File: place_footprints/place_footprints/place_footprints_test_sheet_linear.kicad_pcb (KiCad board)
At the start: 2 copper layers, 64 parts

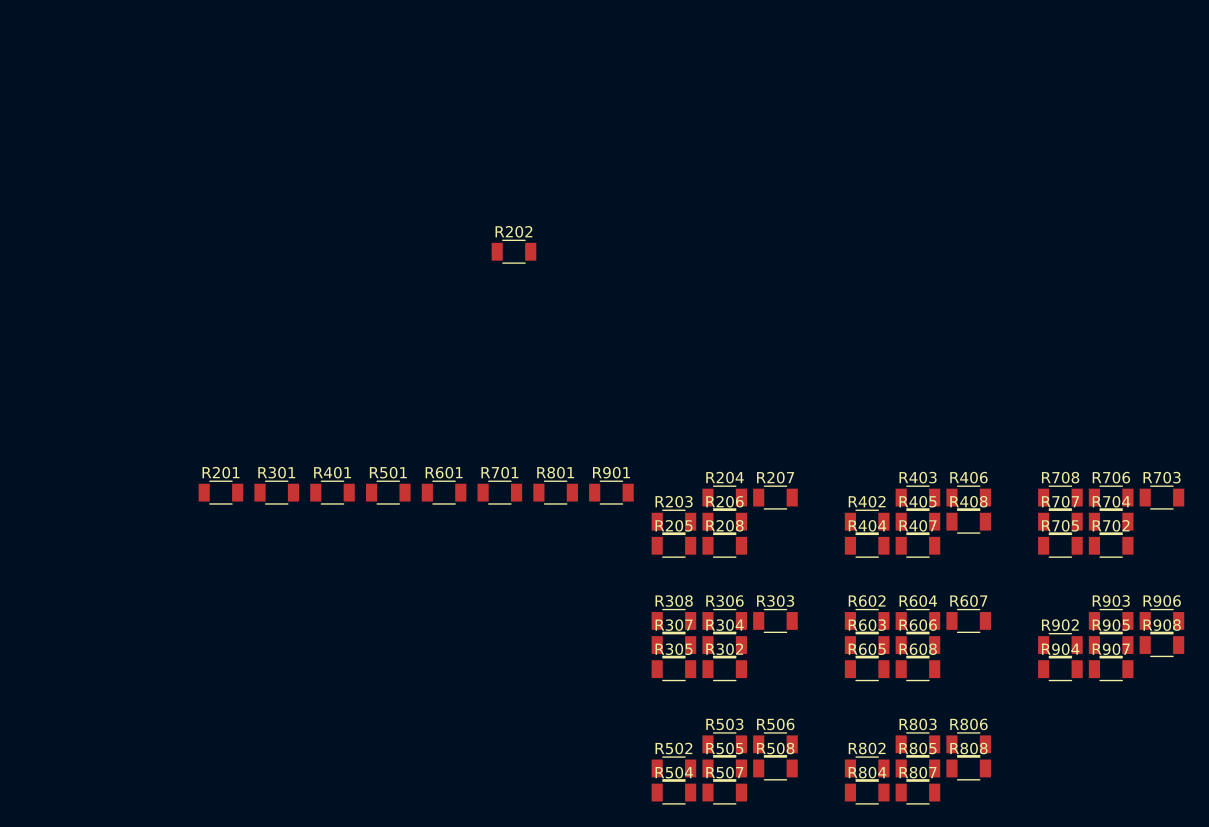
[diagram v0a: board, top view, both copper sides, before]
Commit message: Fixed circular placement
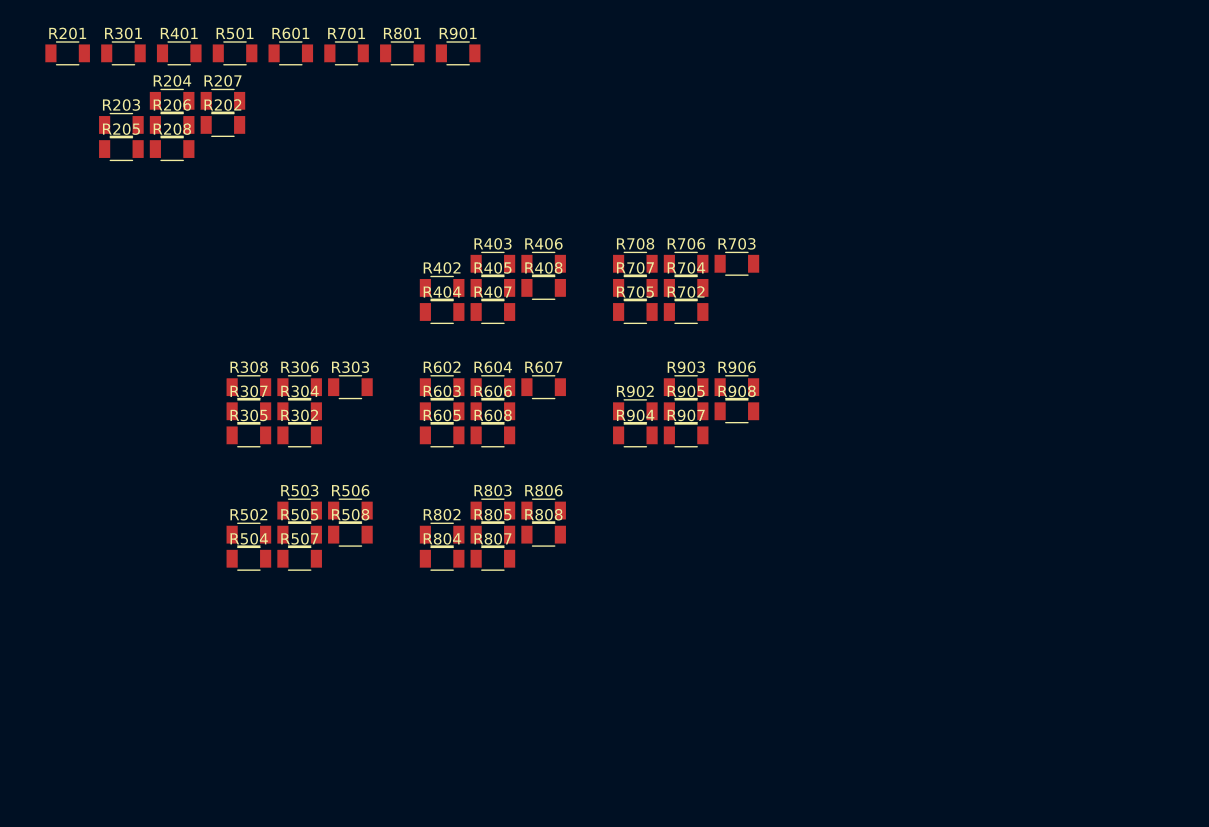
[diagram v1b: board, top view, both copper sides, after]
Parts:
- moved R204 61.0 mm to (53.2, 33.5)
- moved R206 61.0 mm to (53.2, 35.6)
- moved R208 61.0 mm to (53.2, 37.8)
- moved R207 61.0 mm to (57.7, 33.5)
- moved R203 61.0 mm to (48.6, 35.6)
- moved R205 61.0 mm to (48.6, 37.8)
- moved R302 43.5 mm to (64.6, 63.5)
- moved R303 43.5 mm to (69.2, 59.1)
- moved R304 43.5 mm to (64.6, 61.3)
- moved R306 43.5 mm to (64.6, 59.1)
- moved R402 43.5 mm to (77.4, 50.2)
- moved R404 43.5 mm to (77.4, 52.4)
- moved R503 43.5 mm to (64.6, 70.2)
- moved R505 43.5 mm to (64.6, 72.4)
- moved R506 43.5 mm to (69.2, 70.2)
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
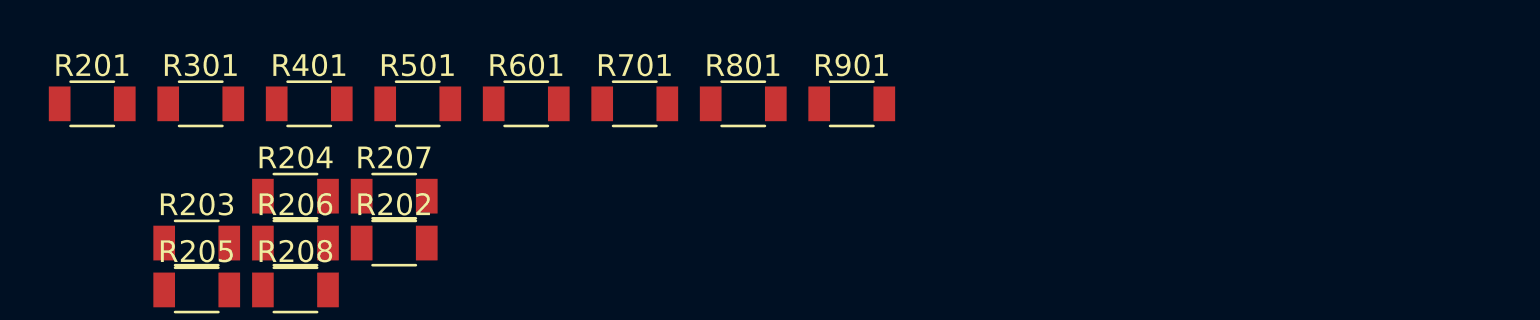
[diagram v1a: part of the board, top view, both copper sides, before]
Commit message: added support for any footprint to serve as a reference in linear and circular mode
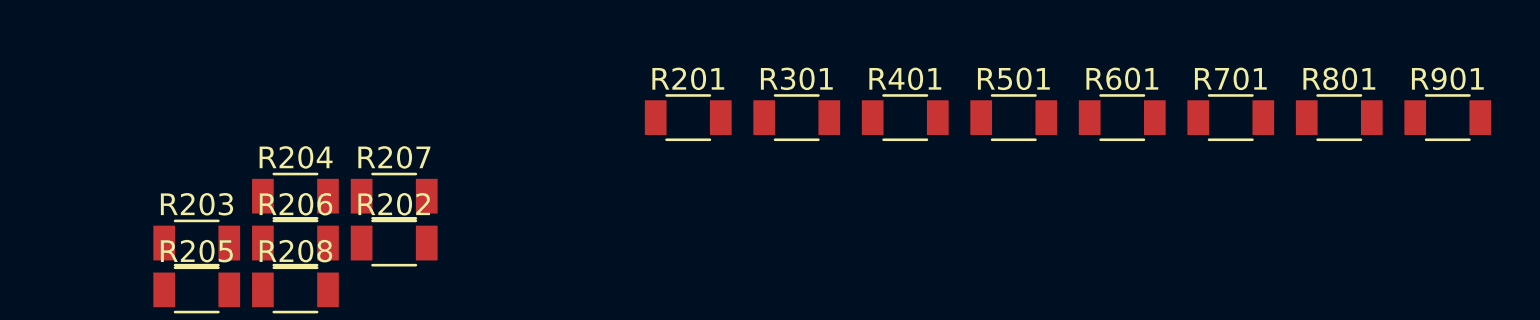
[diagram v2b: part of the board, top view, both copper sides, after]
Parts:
- moved R201 27.5 mm to (71.3, 29.8)
- moved R301 27.5 mm to (76.3, 29.8)
- moved R401 27.5 mm to (81.3, 29.8)
- moved R501 27.5 mm to (86.3, 29.8)
- moved R601 27.5 mm to (91.3, 29.8)
- moved R701 27.5 mm to (96.3, 29.8)
- moved R801 27.5 mm to (101.3, 29.8)
- moved R901 27.5 mm to (106.3, 29.8)
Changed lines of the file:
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@@
-(kicad_pcb (version 20171130) (host pcbnew "(5.0.2)-1")
+(kicad_pcb (version 20171130) (host pcbnew "(5.1.0-rc2-4-g73f0b3087)")
   (general
     (thickness 1.6)
@@
     (zone_45_only no)
     (trace_min 0.2)
-    (segment_width 0.2)
-    (edge_width 0.15)
     (via_size 0.8)
     (via_drill 0.4)
@@
     (uvia_min_size 0.2)
     (uvia_min_drill 0.1)
+    (edge_width 0.15)
+    (segment_width 0.2)
     (pcb_text_width 0.3)
     (pcb_text_size 1.5 1.5)
@@
   )
   (module Passives:R1206M (layer F.Cu)
-    (at 58.815 29.21)
+    (at 86.28 29.845)
     (descr "Capacitor SMD 1206, reflow soldering, AVX (see smccp.pdf)")
     (tags "capacitor 1206")
@@
   )
   (module Passives:R1206M (layer F.Cu)
-    (at 43.815 29.21)
+    (at 71.28 29.845)
     (descr "Capacitor SMD 1206, reflow soldering, AVX (see smccp.pdf)")
     (tags "capacitor 1206")
@@
   )
   (module Passives:R1206M (layer F.Cu)
-    (at 48.815 29.21)
+    (at 76.28 29.845)
     (descr "Capacitor SMD 1206, reflow soldering, AVX (see smccp.pdf)")
     (tags "capacitor 1206")
@@
   )
   (module Passives:R1206M (layer F.Cu)
-    (at 53.815 29.21)
+    (at 81.28 29.845)
     (descr "Capacitor SMD 1206, reflow soldering, AVX (see smccp.pdf)")
     (tags "capacitor 1206")
@@
   )
   (module Passives:R1206M (layer F.Cu)
-    (at 78.815 29.21)
+    (at 106.28 29.845)
     (descr "Capacitor SMD 1206, reflow soldering, AVX (see smccp.pdf)")
     (tags "capacitor 1206")
@@
   )
   (module Passives:R1206M (layer F.Cu)
-    (at 63.815 29.21)
+    (at 91.28 29.845)
     (descr "Capacitor SMD 1206, reflow soldering, AVX (see smccp.pdf)")
     (tags "capacitor 1206")
@@
   )
   (module Passives:R1206M (layer F.Cu)
-    (at 68.815 29.21)
+    (at 96.28 29.845)
     (descr "Capacitor SMD 1206, reflow soldering, AVX (see smccp.pdf)")
     (tags "capacitor 1206")
@@
   )
   (module Passives:R1206M (layer F.Cu)
-    (at 73.815 29.21)
-    (descr "Capacitor SMD 1206, reflow soldering, AVX (see smccp.pdf)")
-    (tags "capacitor 1206")
+    (at 101.28 29.845)
+    (descr "Capacitor SMD 1206, reflow soldering, AVX (see smccp.pdf)")
+    (tags "capacitor 1206")

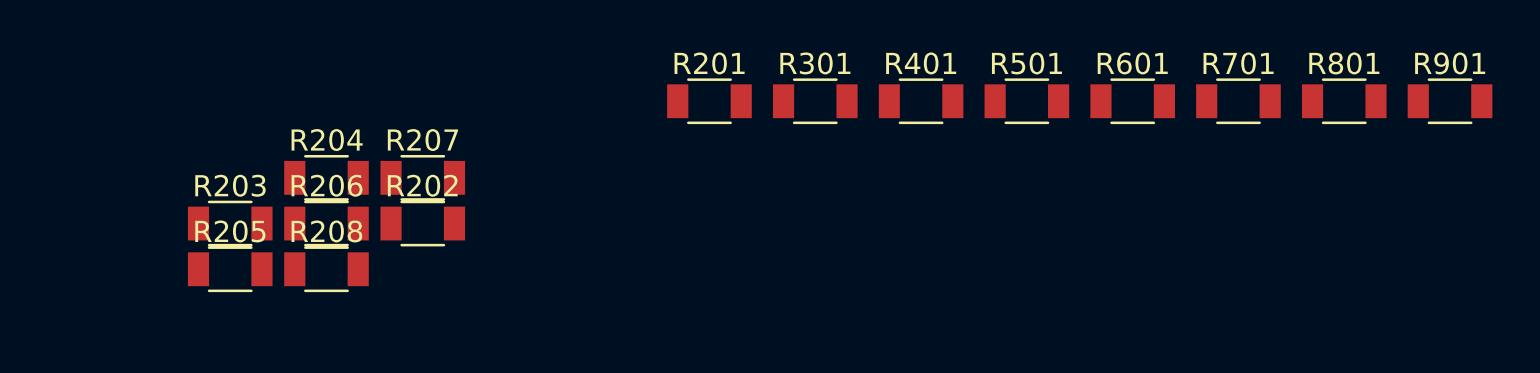
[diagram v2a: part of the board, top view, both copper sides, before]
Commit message: updated test cases
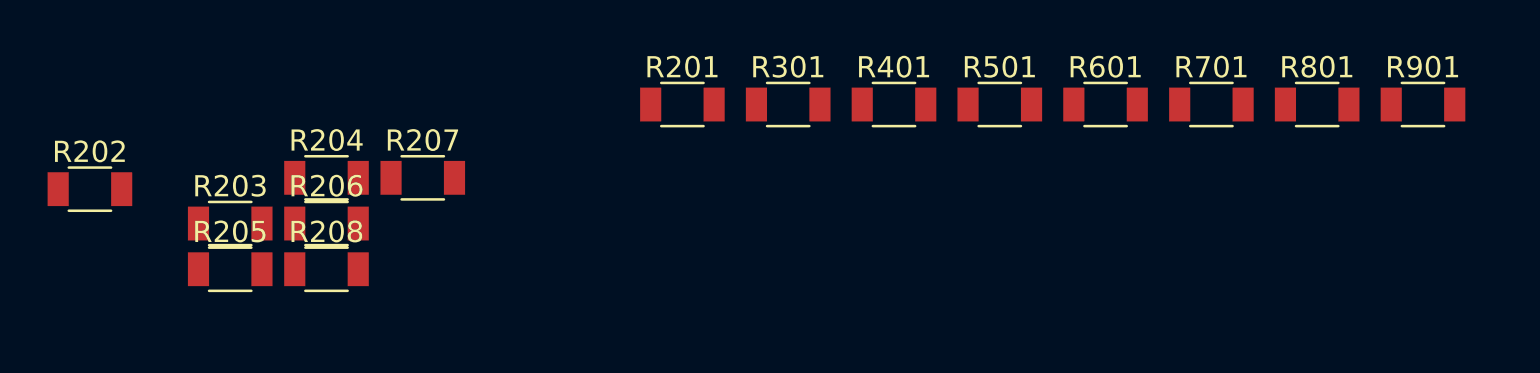
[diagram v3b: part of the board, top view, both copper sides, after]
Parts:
- moved R202 15.8 mm to (42.0, 34.0)
- moved R201 1.29 mm to (70.0, 30.0)
- moved R301 1.29 mm to (75.0, 30.0)
- moved R401 1.29 mm to (80.0, 30.0)
- moved R501 1.29 mm to (85.0, 30.0)
- moved R601 1.29 mm to (90.0, 30.0)
- moved R701 1.29 mm to (95.0, 30.0)
- moved R801 1.29 mm to (100.0, 30.0)
- moved R901 1.29 mm to (105.0, 30.0)
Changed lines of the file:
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@@
-(kicad_pcb (version 20171130) (host pcbnew "(5.1.0-rc2-4-g73f0b3087)")
+(kicad_pcb (version 20171130) (host pcbnew "(5.1.5-90-g5c7ac1bb7)-1")
   (general
     (thickness 1.6)
@@
   )
   (module Passives:R1206M (layer F.Cu)
-    (at 86.28 29.845)
+    (at 85 30)
     (descr "Capacitor SMD 1206, reflow soldering, AVX (see smccp.pdf)")
     (tags "capacitor 1206")
@@
   )
   (module Passives:R1206M (layer F.Cu)
-    (at 71.28 29.845)
+    (at 70 30)
     (descr "Capacitor SMD 1206, reflow soldering, AVX (see smccp.pdf)")
     (tags "capacitor 1206")
@@
   )
   (module Passives:R1206M (layer F.Cu)
-    (at 76.28 29.845)
+    (at 75 30)
     (descr "Capacitor SMD 1206, reflow soldering, AVX (see smccp.pdf)")
     (tags "capacitor 1206")
@@
   )
   (module Passives:R1206M (layer F.Cu)
-    (at 57.730001 35.625001)
+    (at 42 34)
     (descr "Capacitor SMD 1206, reflow soldering, AVX (see smccp.pdf)")
     (tags "capacitor 1206")
@@
   )
   (module Passives:R1206M (layer F.Cu)
-    (at 81.28 29.845)
+    (at 80 30)
     (descr "Capacitor SMD 1206, reflow soldering, AVX (see smccp.pdf)")
     (tags "capacitor 1206")
@@
   )
   (module Passives:R1206M (layer F.Cu)
-    (at 106.28 29.845)
+    (at 105 30)
     (descr "Capacitor SMD 1206, reflow soldering, AVX (see smccp.pdf)")
     (tags "capacitor 1206")
@@
   )
   (module Passives:R1206M (layer F.Cu)
-    (at 91.28 29.845)
+    (at 90 30)
     (descr "Capacitor SMD 1206, reflow soldering, AVX (see smccp.pdf)")
     (tags "capacitor 1206")
@@
   )
   (module Passives:R1206M (layer F.Cu)
-    (at 96.28 29.845)
+    (at 95 30)
     (descr "Capacitor SMD 1206, reflow soldering, AVX (see smccp.pdf)")
     (tags "capacitor 1206")
@@
   )
   (module Passives:R1206M (layer F.Cu)
-    (at 101.28 29.845)
-    (descr "Capacitor SMD 1206, reflow soldering, AVX (see smccp.pdf)")
-    (tags "capacitor 1206")
+    (at 100 30)
+    (descr "Capacitor SMD 1206, reflow soldering, AVX (see smccp.pdf)")
+    (tags "capacitor 1206")
